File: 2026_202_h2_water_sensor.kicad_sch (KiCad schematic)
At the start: 0 parts

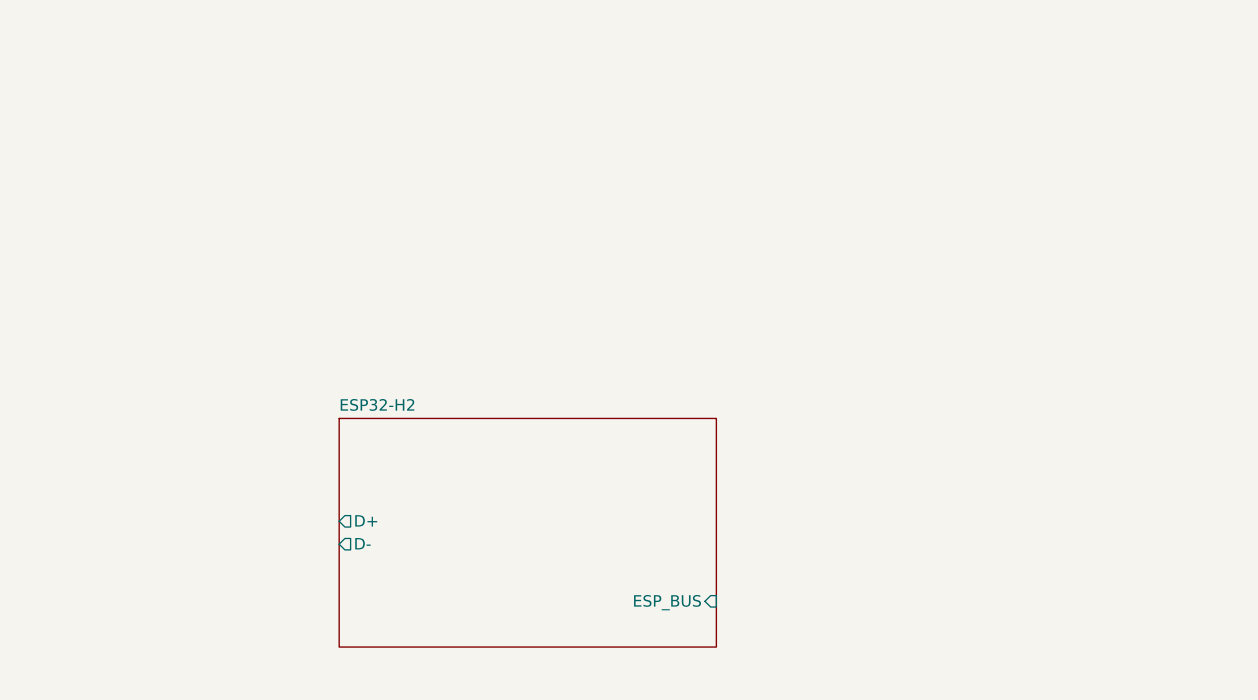
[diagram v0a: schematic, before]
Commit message: H2-Board: C6/S3-Werkbank-Blätter raus, H2-Subsheet auf neuen Block-Stand (ESP32-H2-MINI-1-N4)
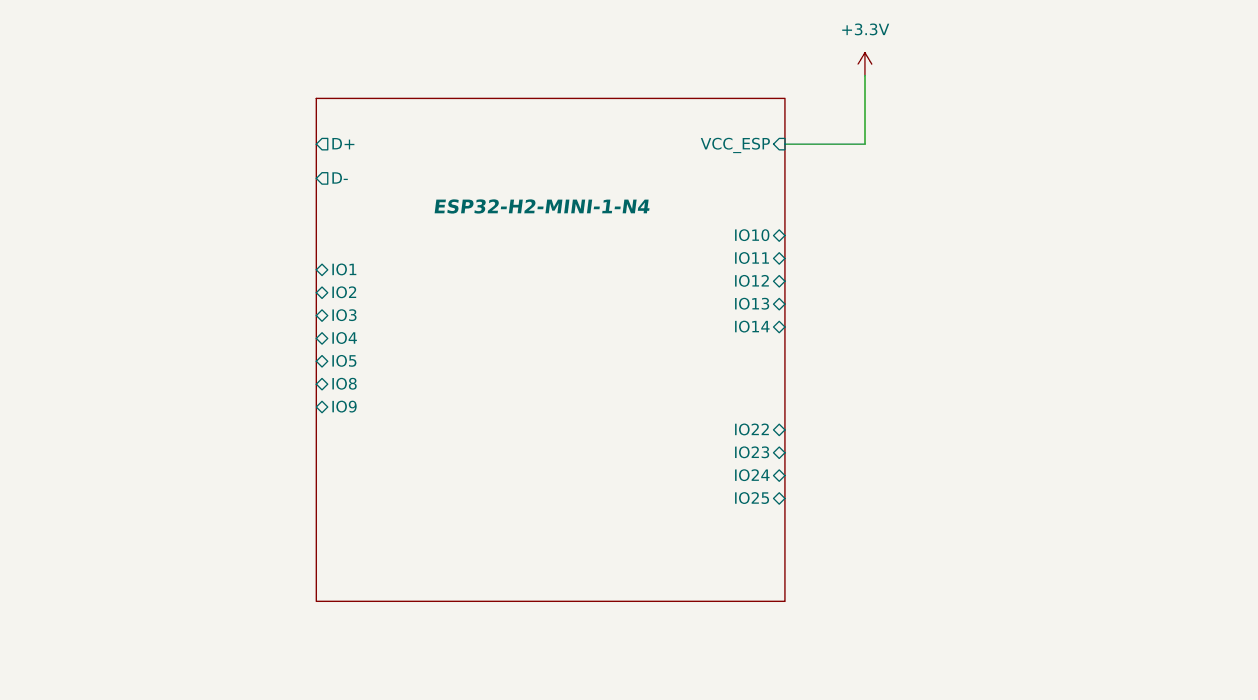
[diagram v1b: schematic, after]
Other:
- removed sheet ESP32-H2
- added sheet ESP32-H2-MINI-1-N4 (ESP32-H2-MINI-1-N4.kicad_sch)

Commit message: Migration PCM_JLCPCB- -> JLCPCB_ (Symbole aus Submodule)
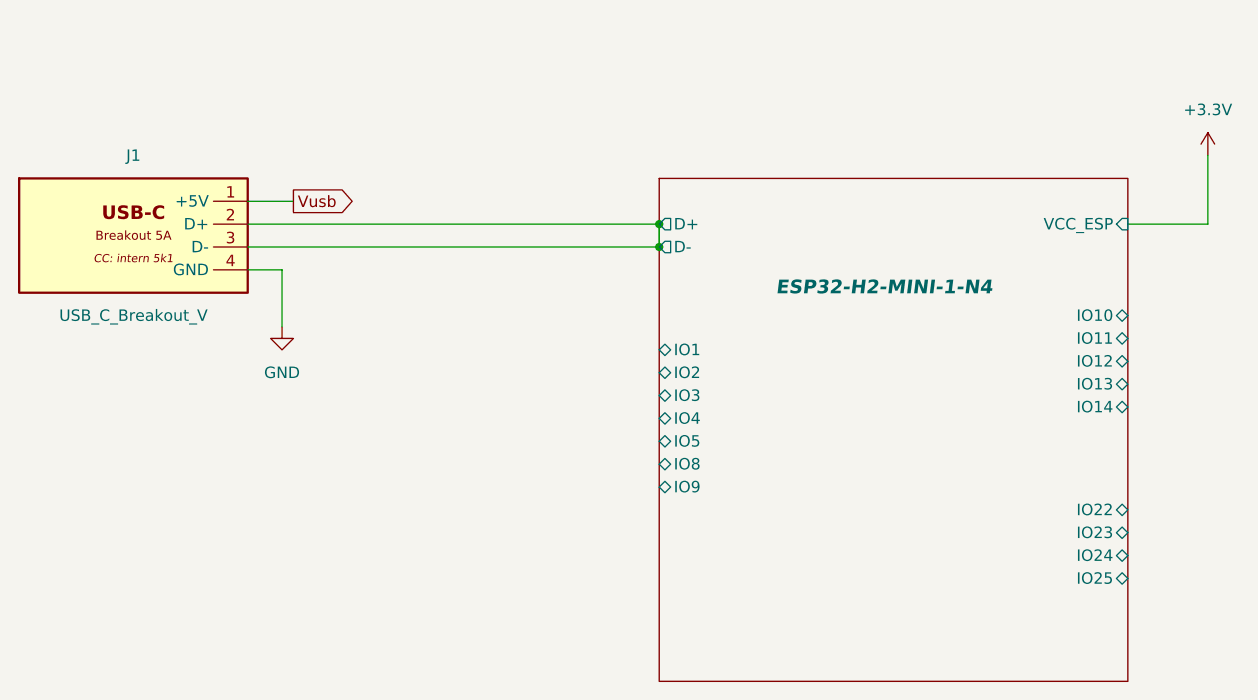
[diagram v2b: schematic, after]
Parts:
- added J1: USB_C_Breakout_V, jlcpcb:CONN-SMD_BM04B-SRSS-TB, symbol DL1DTU_USB_C_Breakout_V:USB_C_Breakout_V
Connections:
- net ESP32-H2-MINI-1-N4/D+: now also J1.2 (D+), J1.3 (D-)
- new net GND: J1.4 (GND)
- new net Vusb: J1.1 (+5V)
